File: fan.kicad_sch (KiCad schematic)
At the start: 14 parts, among them J6 Conn_01x04, U10 EMC2101

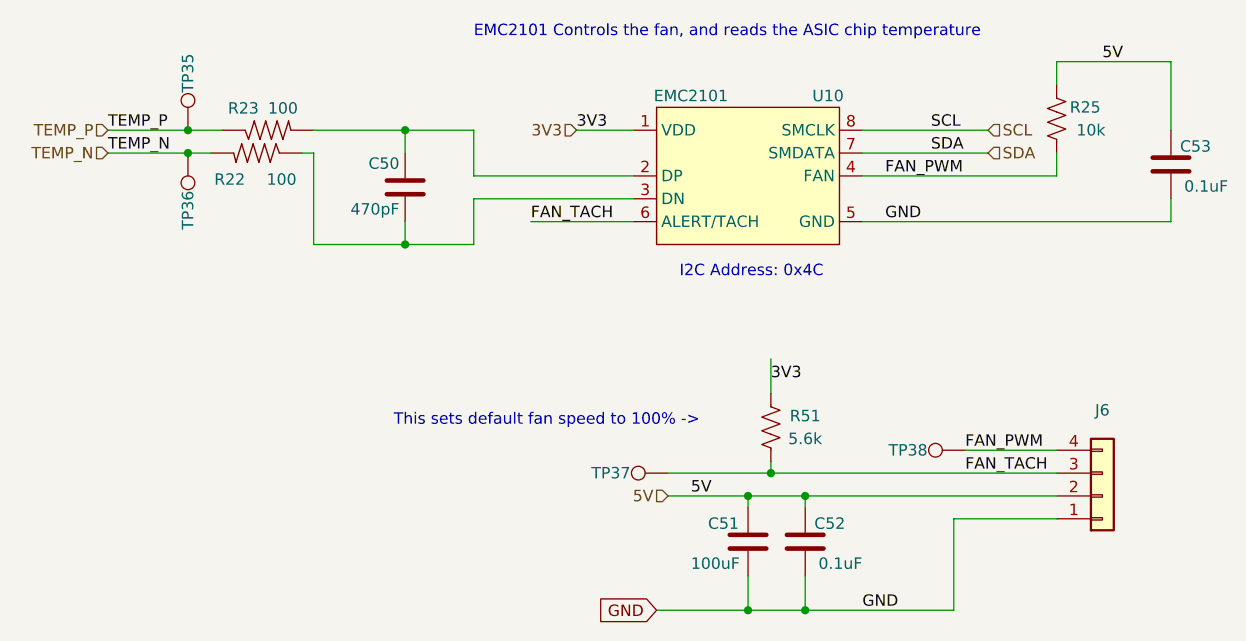
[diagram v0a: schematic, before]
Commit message: added DK partnumbers and exported BOM
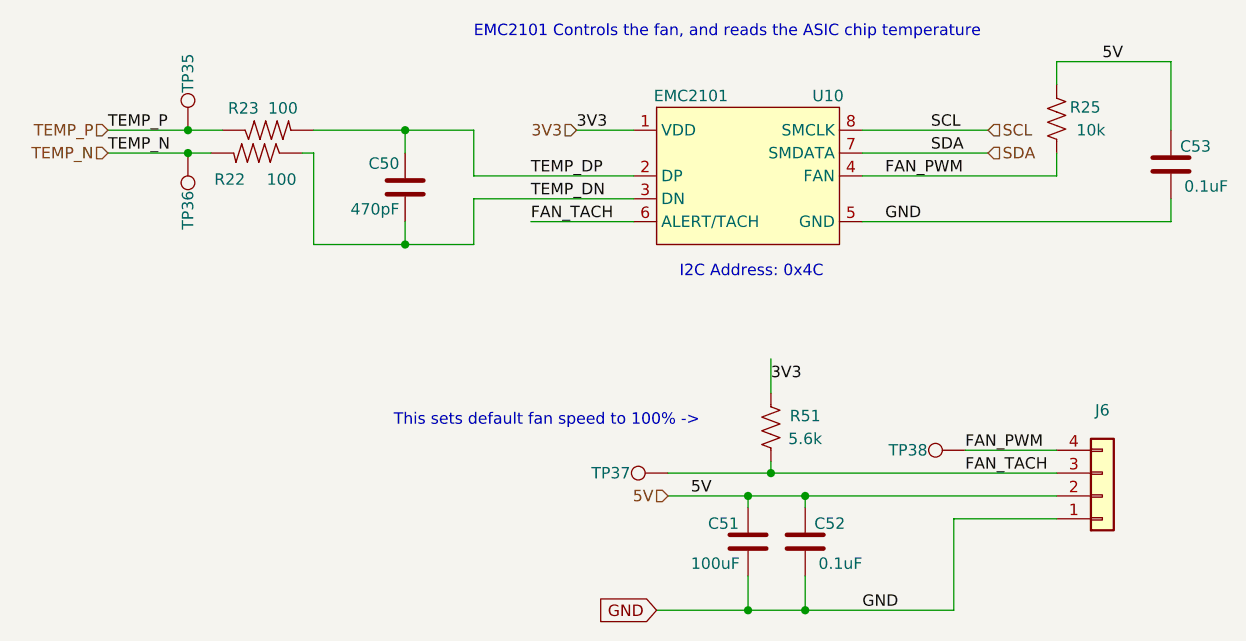
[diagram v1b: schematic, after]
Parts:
- C51: DK 490-9969-1-ND -> 490-6533-1-ND; PARTNO GRM32ER61A107ME20L -> GRM32EC80J107ME20L
- C53: DK 478-KGM05AR71C104KHTR-ND -> 1292-1639-1-ND; PARTNO KGM05AR71C104KH -> 0402X104K100CT
- R22, R23: DK RMCF0402FT100RCT-ND -> 311-100LRCT-ND; PARTNO RMCF0402FT100R -> RC0402FR-07100RL
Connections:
- net TEMP_DN: now reaches C50.2, R22.1, U10.3 (DN)
- net TEMP_DP: now reaches C50.1, R23.2, U10.2 (DP)
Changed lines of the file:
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@@
+		)
+	)
+	(label "TEMP_DN"
+		(at 120.65 81.28 0)
+		(fields_autoplaced yes)
+		(effects
+			(font
+				(size 1.27 1.27)
+			)
+			(justify left bottom)
 		)
 	)
@@
 	(label "SDA"
 		(at 165.1 76.2 0)
+		(fields_autoplaced yes)
+		(effects
+			(font
+				(size 1.27 1.27)
+			)
+			(justify left bottom)
+		)
+	)
+	(label "TEMP_DP"
+		(at 120.65 78.74 0)
 		(fields_autoplaced yes)
 		(effects
@@
 			)
 		)
-		(property "DK" "478-KGM05AR71C104KHTR-ND"
+		(property "DK" "1292-1639-1-ND"
 			(at 191.77 77.47 0)
 			(effects
@@
 			)
 		)
-		(property "PARTNO" "KGM05AR71C104KH"
+		(property "PARTNO" "0402X104K100CT"
 			(at 191.77 77.47 0)
 			(effects
@@
 			)
 		)
-		(property "DK" "RMCF0402FT100RCT-ND"
+		(property "DK" "311-100LRCT-ND"
 			(at 90.17 76.2 0)
 			(effects
@@
 			)
 		)
-		(property "PARTNO" "RMCF0402FT100R"
+		(property "PARTNO" "RC0402FR-07100RL"
 			(at 90.17 76.2 0)
 			(effects
@@
 			)
 		)
-		(property "DK" "490-9969-1-ND"
+		(property "DK" "490-6533-1-ND"
 			(at 144.78 119.38 0)
 			(effects
@@
 			)
 		)
-		(property "PARTNO" "GRM32ER61A107ME20L"
+		(property "PARTNO" "GRM32EC80J107ME20L"
 			(at 144.78 119.38 0)
 			(effects
@@
 			)
 		)
-		(property "DK" "RMCF0402FT100RCT-ND"
+		(property "DK" "311-100LRCT-ND"
 			(at 91.44 73.66 0)
 			(effects
@@
 			)
 		)
-		(property "PARTNO" "RMCF0402FT100R"
+		(property "PARTNO" "RC0402FR-07100RL"
 			(at 91.44 73.66 0)
 			(effects

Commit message: swapped some parts numbers and packages for #169, DFM Improvements
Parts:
- C51: footprint Capacitor_SMD:C_1210_3225Metric -> Capacitor_SMD:C_1206_3216Metric; DK 490-6533-1-ND -> 445-6008-1-ND; PARTNO GRM32EC80J107ME20L -> C3216X5R0J107M160AB
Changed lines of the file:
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@@
 			)
 		)
-		(property "Footprint" "Capacitor_SMD:C_1210_3225Metric"
+		(property "Footprint" "Capacitor_SMD:C_1206_3216Metric"
 			(at 144.78 119.38 0)
 			(effects
@@
 			)
 		)
-		(property "DK" "490-6533-1-ND"
+		(property "DK" "445-6008-1-ND"
 			(at 144.78 119.38 0)
 			(effects
@@
 			)
 		)
-		(property "PARTNO" "GRM32EC80J107ME20L"
+		(property "PARTNO" "C3216X5R0J107M160AB"
 			(at 144.78 119.38 0)
 			(effects

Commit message: silkscreen cleanup
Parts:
- C51: DK 445-6008-1-ND -> 490-GRM31CR61A107MEA8LCT-ND; PARTNO C3216X5R0J107M160AB -> GRM31CR61A107MEA8L
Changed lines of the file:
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@@
 			)
 		)
-		(property "DK" "445-6008-1-ND"
+		(property "DK" "490-GRM31CR61A107MEA8LCT-ND"
 			(at 144.78 119.38 0)
 			(effects
@@
 			)
 		)
-		(property "PARTNO" "C3216X5R0J107M160AB"
+		(property "PARTNO" "GRM31CR61A107MEA8L"
 			(at 144.78 119.38 0)
 			(effects

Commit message: caps, back plane
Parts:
- C51: value 100uF -> 47uF; footprint Capacitor_SMD:C_1206_3216Metric -> Capacitor_SMD:C_1210_3225Metric; DK 490-GRM31CR61A107MEA8LCT-ND -> 1276-3376-1-ND; PARTNO GRM31CR61A107MEA8L -> CL32A476KOJNNNE
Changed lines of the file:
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@@
 			)
 		)
-		(property "Value" "100uF"
+		(property "Value" "47uF"
 			(at 138.43 122.555 0)
 			(effects
@@
 			)
 		)
-		(property "Footprint" "Capacitor_SMD:C_1206_3216Metric"
+		(property "Footprint" "Capacitor_SMD:C_1210_3225Metric"
 			(at 144.78 119.38 0)
 			(effects
@@
 			)
 		)
-		(property "DK" "490-GRM31CR61A107MEA8LCT-ND"
+		(property "DK" "1276-3376-1-ND"
 			(at 144.78 119.38 0)
 			(effects
@@
 			)
 		)
-		(property "PARTNO" "GRM31CR61A107MEA8L"
+		(property "PARTNO" "CL32A476KOJNNNE"
 			(at 144.78 119.38 0)
 			(effects

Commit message: normalized 0.1uF capacitor part numbers
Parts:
- C52, C53: DK 1292-1639-1-ND -> 1276-1234-1-ND; PARTNO 0402X104K100CT -> CL05A104KO5NNNC
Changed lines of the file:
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@@
 			)
 		)
-		(property "DK" "1292-1639-1-ND"
+		(property "DK" "1276-1234-1-ND"
 			(at 191.77 77.47 0)
 			(effects
@@
 			)
 		)
-		(property "PARTNO" "0402X104K100CT"
+		(property "PARTNO" "CL05A104KO5NNNC"
 			(at 191.77 77.47 0)
 			(effects
@@
 			)
 		)
-		(property "DK" "1292-1639-1-ND"
+		(property "DK" "1276-1234-1-ND"
 			(at 151.13 119.38 0)
 			(effects
@@
 			)
 		)
-		(property "PARTNO" "0402X104K100CT"
+		(property "PARTNO" "CL05A104KO5NNNC"
 			(at 151.13 119.38 0)
 			(effects
